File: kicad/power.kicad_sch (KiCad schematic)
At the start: 39 parts, among them J1 USB_C_Receptacle_USB2.0_16P, J3 XT30PW-M, Q1 AO4407A, SW1 Power, U4 AP64500SP-13, U8 HT7550-1, U9 XC6206P332MR

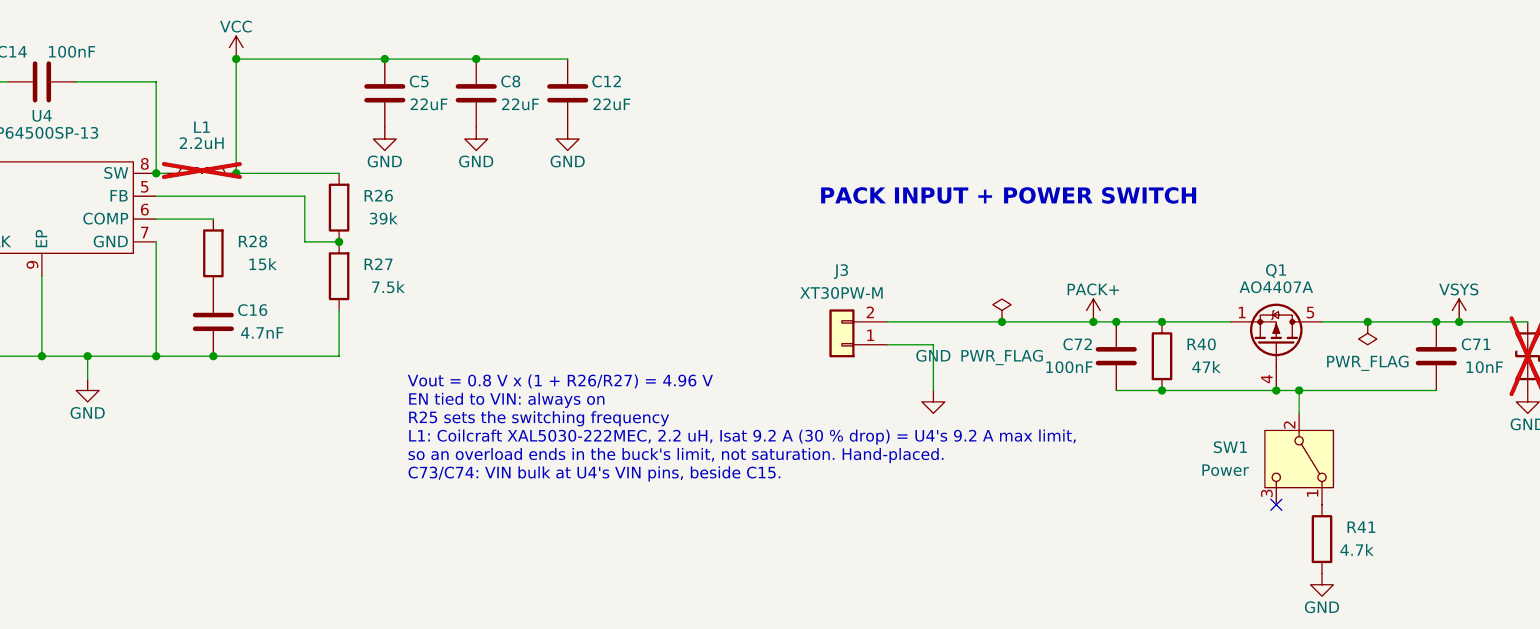
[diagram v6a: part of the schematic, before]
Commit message: Replace the RP2354 core inductor with a 1.1 V LDO and fix JLC placements
L3 (the Abracon AOTA-B201610S3R3-101-T, the only polarity-marked inductor
RPi approves) had 3 in stock at JLC. DVDD now comes from U12, a TLV74311
LDO on +3V3 with C87/C86, as in RP2350 datasheet Fig. 24: VREG_FB to GND,
VREG_LX open, VREG_VIN and VREG_AVDD still powered. Firmware must set the
VREG HIZ bit after boot and never use the regulator's low-power mode.

- Schematic, placement, recipe, grid router and DRU updated; the copper
  is rebuilt with route_all. DRC, ERC and parity are clean.
- fab.py: JLC rotation offsets for the JST PH connectors, J3's XT30 and
  SW1 (all 180 degrees), and U8 placed at its pad centre, from JLC's
  placement preview. The JLC quote is $269.19 for 5 panels.
- Unused footprints removed (L_Abracon_AOTA-B201610, the trimmed 0402),
  along with the cleanup session's footprint, symbol, branch and build/
  tidy-up, and its renders/, docs/ and tools/case/ moves.

Co-Authored-By: Claude Opus 5.5 <noreply@anthropic.com>
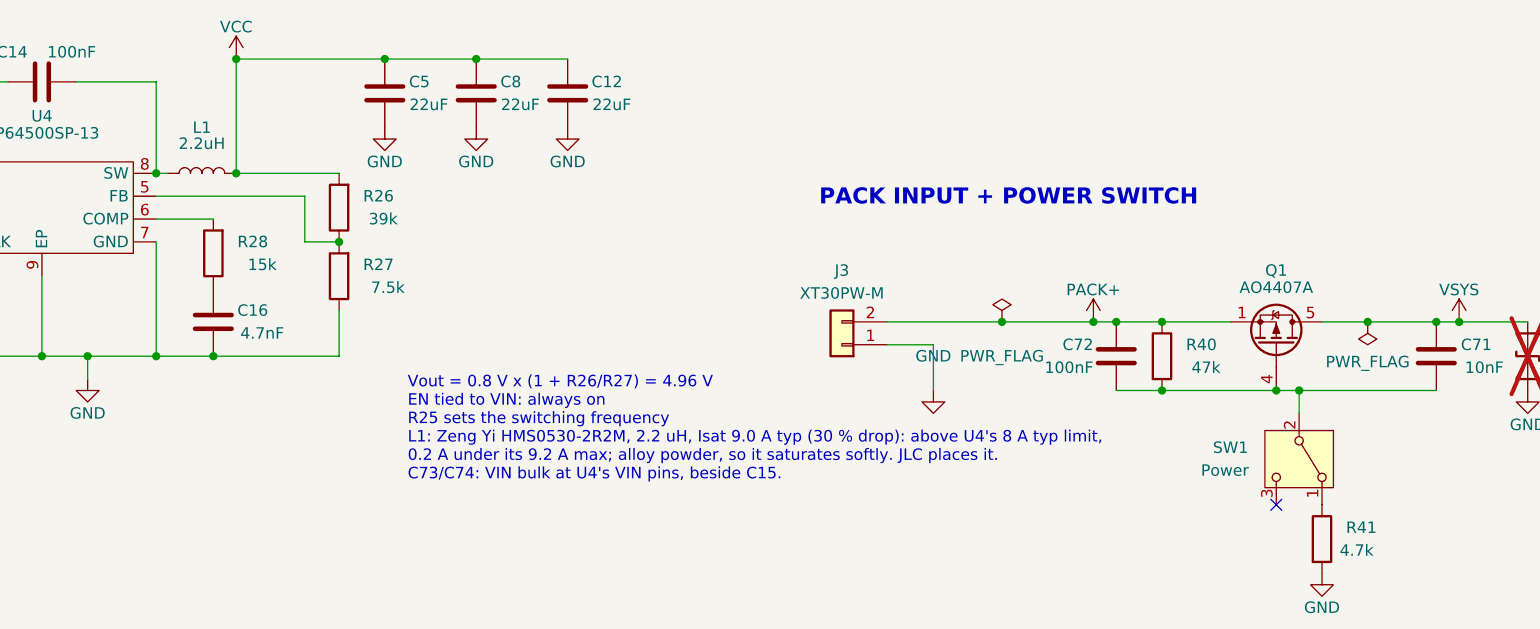
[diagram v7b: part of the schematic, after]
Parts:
- C74: LCSC Part # C1525 -> C307331; MPN CL05B104KO5NNNC -> CL05B104KB54PNC
- L1: footprint hexy:L_Coilcraft_XAL5030 -> hexy:L_ZengYi_HMS0530; LCSC Part # C920280 -> C18734448; MPN XAL5030-222MEC -> HMS0530-2R2M; Manufacturer Coilcraft -> Zeng Yi; now fitted
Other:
- note added: "Vout = 0.8 V x (1 + R26/R27) = 4.96 V EN tied to VIN: always on R25 sets the switching frequency L1: Zeng Yi HMS0530-2R2M, 2.2 uH, Isat 9.0 A typ (30 % drop): above U4's 8 A typ limit, 0.2 A under its 9.2 A max; alloy powder, so it saturates softly. JLC places it. C73/C74: VIN bulk at U4's VIN pins, beside C15."
- note removed: "Vout = 0.8 V x (1 + R26/R27) = 4.96 V EN tied to VIN: always on R25 sets the switching frequency L1: Coilcraft XAL5030-222MEC, 2.2 uH, Isat 9.2 A (30 % drop) = U4's 9.2 A max limit, so an overload ends in the buck's limit, not saturation. Hand-placed. C73/C74: VIN bulk at U4's VIN pins, beside C15."
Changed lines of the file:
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@@
 		)
 	)
-	(text "Vout = 0.8 V x (1 + R26/R27) = 4.96 V\nEN tied to VIN: always on\nR25 sets the switching frequency\nL1: Coilcraft XAL5030-222MEC, 2.2 uH, Isat 9.2 A (30 % drop) = U4's 9.2 A max limit,\nso an overload ends in the buck's limit, not saturation. Hand-placed.\nC73/C74: VIN bulk at U4's VIN pins, beside C15."
+	(text "Vout = 0.8 V x (1 + R26/R27) = 4.96 V\nEN tied to VIN: always on\nR25 sets the switching frequency\nL1: Zeng Yi HMS0530-2R2M, 2.2 uH, Isat 9.0 A typ (30 % drop): above U4's 8 A typ limit,\n0.2 A under its 9.2 A max; alloy powder, so it saturates softly. JLC places it.\nC73/C74: VIN bulk at U4's VIN pins, beside C15."
 		(exclude_from_sim no)
 		(at 106.68 187.96 0)
@@
 		(on_board yes)
 		(in_pos_files yes)
-		(dnp yes)
+		(dnp no)
 		(fields_autoplaced yes)
 		(property "Reference" "L1"
@@
 			)
 		)
-		(property "Footprint" "hexy:L_Coilcraft_XAL5030"
+		(property "Footprint" "hexy:L_ZengYi_HMS0530"
 			(at 83.82 153.67 0)
 			(hide yes)
@@
 			)
 		)
-		(property "Datasheet" ""
+		(property "Datasheet" "https://jlcpcb.com/api/file/downloadByFileSystemAccessId/8757789949045420032"
 			(at 83.82 153.67 0)
 			(hide yes)
@@
 			)
 		)
-		(property "LCSC Part #" "C920280"
+		(property "LCSC Part #" "C18734448"
 			(at -80.0101 236.2201 0)
 			(hide yes)
@@
 			)
 		)
-		(property "MPN" "XAL5030-222MEC"
+		(property "MPN" "HMS0530-2R2M"
 			(at 83.82 153.67 0)
 			(hide yes)
@@
 			)
 		)
-		(property "Manufacturer" "Coilcraft"
+		(property "Manufacturer" "Zeng Yi"
 			(at 83.82 153.67 0)
 			(hide yes)
@@
 			)
 		)
-		(property "LCSC Part #" "C1525"
+		(property "LCSC Part #" "C307331"
 			(at 57.1501 335.2801 0)
 			(hide yes)
@@
 			)
 		)
-		(property "MPN" "CL05B104KO5NNNC"
+		(property "MPN" "CL05B104KB54PNC"
 			(at 16.51 162.56 0)
 			(hide yes)

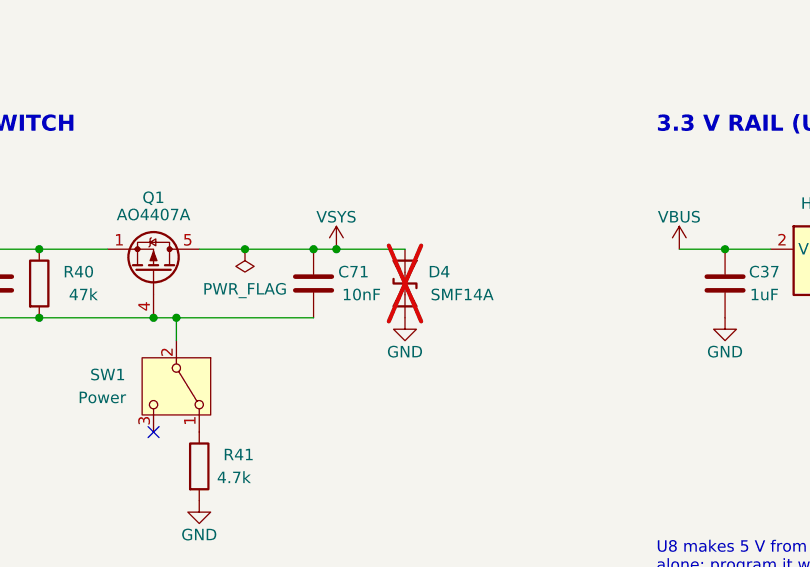
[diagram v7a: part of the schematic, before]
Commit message: Have JLC place SW2, D4, U14 and F2, and shift U8 onto its model
- SW2 (BOOT), D4, U14 and F2 were DNP for hand placement. All four are
  in stock at JLC, so they're placed now (DNP cleared in the schematic
  and on the board). The JLC BOM grows from 47 to 51 lines.
- fab.py: JLC's SOT-89-3 model for U8 (C16106) sits 0.474 mm toward the
  tab from its footprint origin, so U8's CPL point moves that far toward
  its pins (JLC_PART_SHIFT), replacing the pad-centre approximation.
- The 10-panel JLC quote is $331.69, and the preview shows all five parts
  correct.

Co-Authored-By: Claude Opus 5.5 <noreply@anthropic.com>
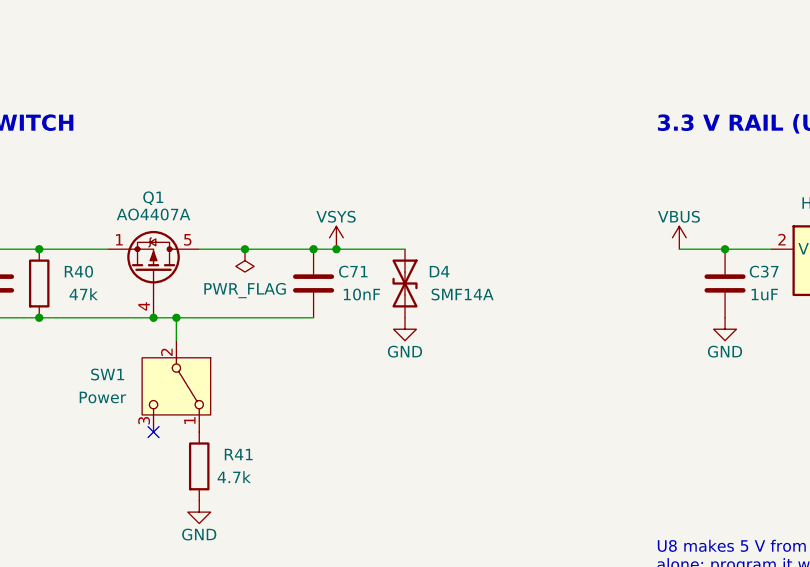
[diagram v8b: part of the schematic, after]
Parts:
- D4: now fitted
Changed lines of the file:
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@@
 		(on_board yes)
 		(in_pos_files yes)
-		(dnp yes)
+		(dnp no)
 		(property "Reference" "D4"
 			(at 234.95 172.72 90)
